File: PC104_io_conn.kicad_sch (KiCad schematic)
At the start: 1 part, among them P651 Conn_04x26_Pin

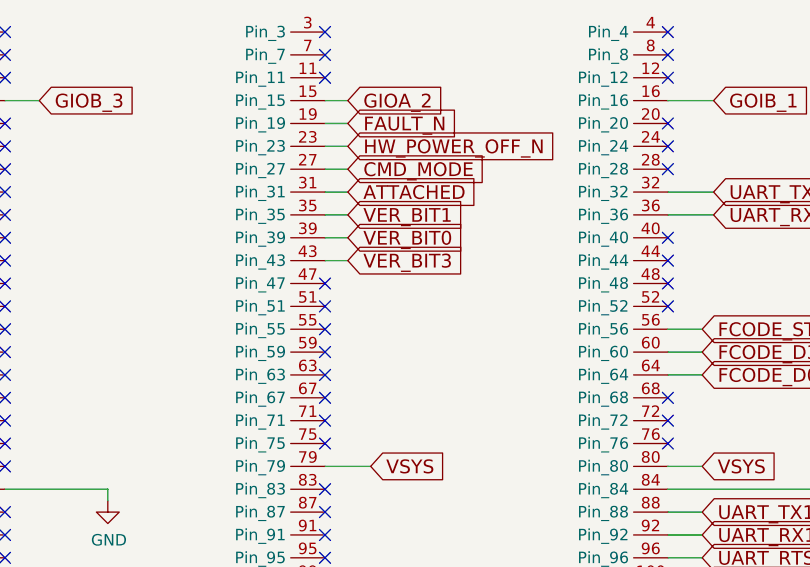
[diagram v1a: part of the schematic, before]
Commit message: Clean up RTC, start working on power
Signed-off-by: Corey Minyard <corey@minyard.net>
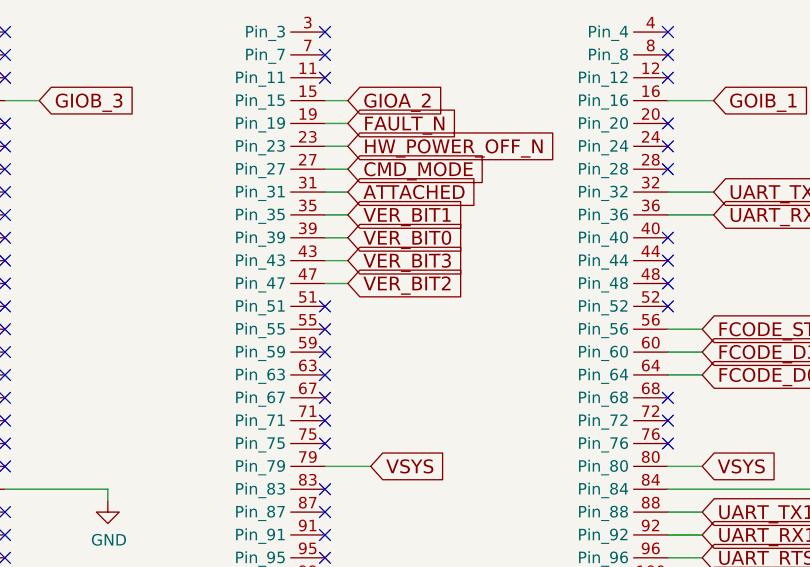
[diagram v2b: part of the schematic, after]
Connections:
- net VER_BIT2: now reaches P651.47 (Pin_47)
- no-connect marks 74 -> 73
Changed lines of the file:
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@@
-	)
-	(no_connect
-		(at 182.88 96.52)
 	)
 	(no_connect
@@
 	(wire
 		(pts
+			(xy 182.88 96.52) (xy 185.42 96.52)
+		)
+		(stroke
+			(width 0)
+			(type default)
+		)
+	)
+	(wire
+		(pts
 			(xy 109.22 96.52) (xy 113.03 96.52)
 		)
@@
 		)
 	)
+	(global_label "VER_BIT2"
+		(shape input)
+		(at 185.42 96.52 0)
+		(fields_autoplaced yes)
+		(effects
+			(font
+				(size 1.524 1.524)
+			)
+			(justify left)
+		)
+		(property "Intersheetrefs" "${INTERSHEET_REFS}"
+			(at 198.4493 96.52 0)
+			(effects
+				(font
+					(size 1.27 1.27)
+				)
+				(justify left)
+				(hide yes)
+			)
+		)
+	)

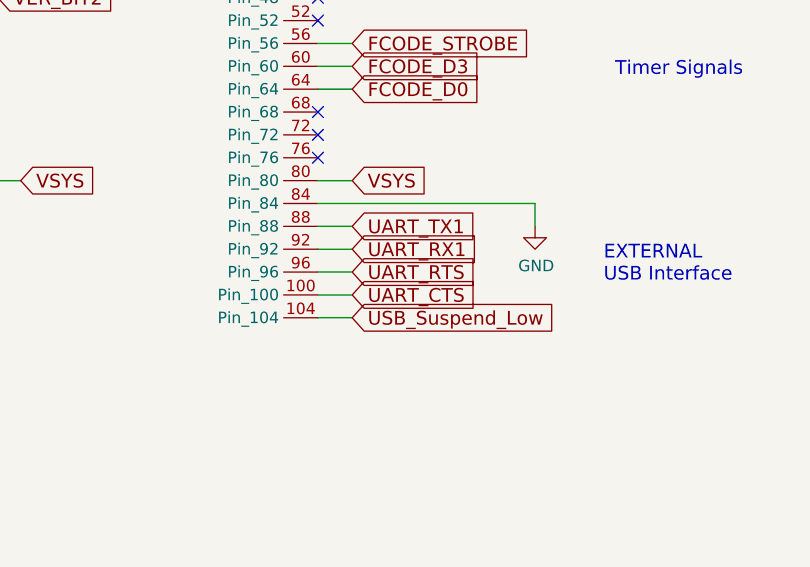
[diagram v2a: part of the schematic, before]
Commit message: More cleanup, finish hooking up power supply controls
Signed-off-by: Corey Minyard <corey@minyard.net>
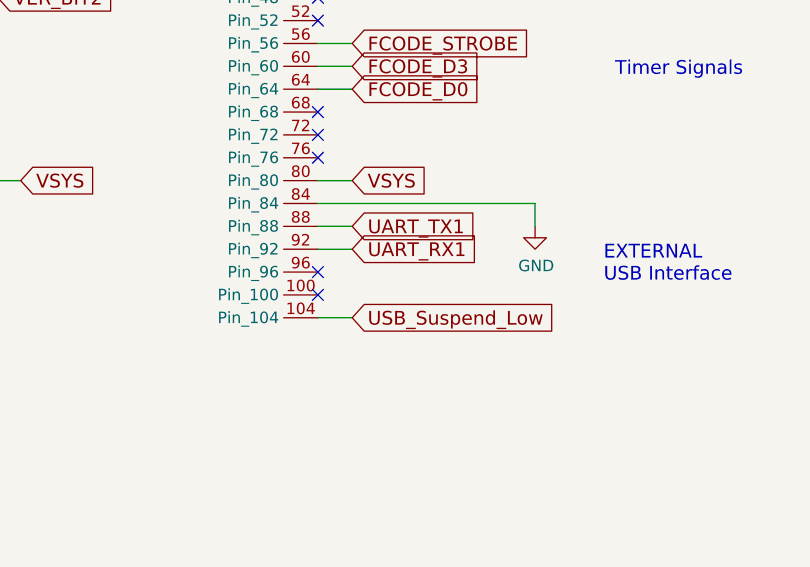
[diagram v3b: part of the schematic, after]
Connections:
- net UART_CTS: no longer names the net of P651.100 (Pin_100)
- net UART_RTS: no longer names the net of P651.96 (Pin_96)
- no-connect marks 73 -> 75
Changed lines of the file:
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@@
+	)
+	(no_connect
+		(at 220.98 129.54)
 	)
 	(no_connect
@@
 	)
 	(no_connect
+		(at 220.98 127)
+	)
+	(no_connect
 		(at 109.22 91.44)
 	)
@@
 	(wire
 		(pts
-			(xy 220.98 127) (xy 224.79 127)
-		)
-		(stroke
-			(width 0)
-			(type default)
-		)
-	)
-	(wire
-		(pts
 			(xy 119.38 69.85) (xy 119.38 73.66)
 		)
@@
 	(wire
 		(pts
-			(xy 220.98 129.54) (xy 224.79 129.54)
-		)
-		(stroke
-			(width 0)
-			(type default)
-		)
-	)
-	(wire
-		(pts
 			(xy 182.88 86.36) (xy 185.42 86.36)
 		)
@@
 		)
 	)
-	(global_label "UART_RTS"
-		(shape input)
-		(at 224.79 127 0)
-		(fields_autoplaced yes)
-		(effects
-			(font
-				(size 1.524 1.524)
-			)
-			(justify left)
-		)
-		(property "Intersheetrefs" "${INTERSHEET_REFS}"
-			(at 238.377 127 0)
-			(effects
-				(font
-					(size 1.27 1.27)
-				)
-				(justify left)
-				(hide yes)
-			)
-		)
-	)
 	(global_label "VER_BIT1"
 		(shape input)
@@
 			(effects
 				(font
-					(size 1.27 1.27)
-				)
-				(justify left)
-				(hide yes)
-			)
-		)
-	)
-	(global_label "UART_CTS"
-		(shape input)
-		(at 224.79 129.54 0)
-		(fields_autoplaced yes)
-		(effects
-			(font
-				(size 1.524 1.524)
-			)
-			(justify left)
-		)
-		(property "Intersheetrefs" "${INTERSHEET_REFS}"
-			(at 238.377 129.54 0)
-			(effects
-				(font

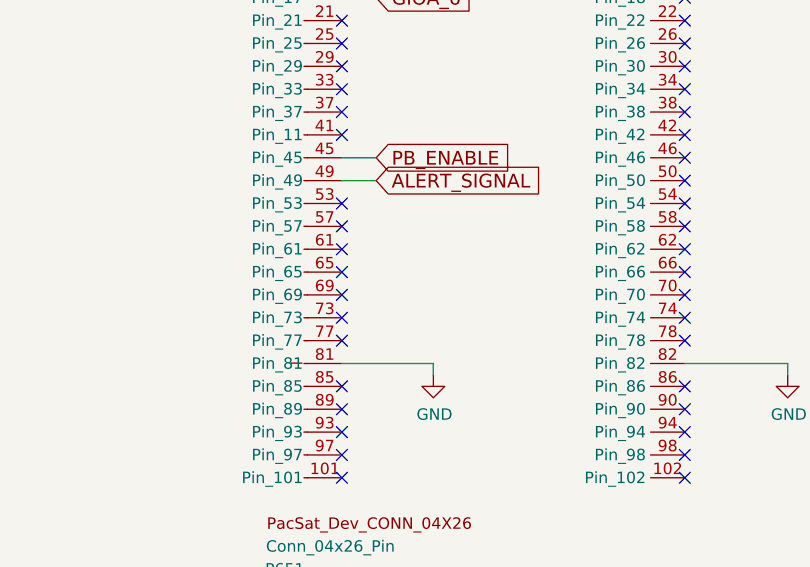
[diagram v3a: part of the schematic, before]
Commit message: Add resistors to the JTAG interface
They are supposed to be there.

Signed-off-by: Corey Minyard <corey@minyard.net>
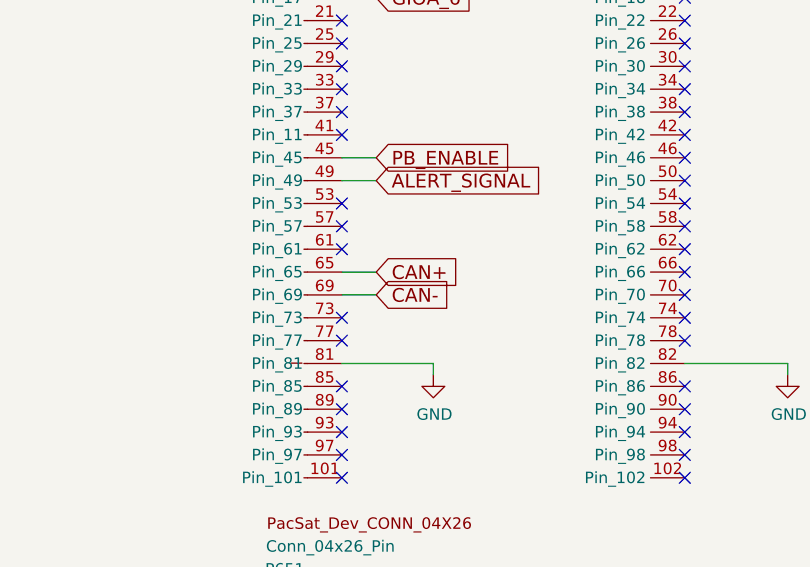
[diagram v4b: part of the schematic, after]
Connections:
- net CAN+: now reaches P651.65 (Pin_65)
- net CAN-: now reaches P651.69 (Pin_69)
- no-connect marks 75 -> 73
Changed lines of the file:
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@@
-	)
-	(no_connect
-		(at 109.22 111.76)
 	)
 	(no_connect
@@
 	)
 	(no_connect
-		(at 109.22 109.22)
-	)
-	(no_connect
 		(at 220.98 81.28)
 	)
@@
 	(wire
 		(pts
+			(xy 109.22 109.22) (xy 113.03 109.22)
+		)
+		(stroke
+			(width 0)
+			(type default)
+		)
+	)
+	(wire
+		(pts
 			(xy 109.22 99.06) (xy 113.03 99.06)
 		)
@@
 		(pts
 			(xy 220.98 121.92) (xy 224.79 121.92)
+		)
+		(stroke
+			(width 0)
+			(type default)
+		)
+	)
+	(wire
+		(pts
+			(xy 109.22 111.76) (xy 113.03 111.76)
 		)
 		(stroke
@@
 			(effects
 				(font
+					(size 1.27 1.27)
+				)
+				(justify left)
+				(hide yes)
+			)
+		)
+	)
+	(global_label "CAN+"
+		(shape input)
+		(at 113.03 109.22 0)
+		(fields_autoplaced yes)
+		(effects
+			(font
+				(size 1.524 1.524)
+			)
+			(justify left)
+		)
+		(property "Intersheetrefs" "${INTERSHEET_REFS}"
+			(at 122.1406 109.22 0)
+			(effects
+				(font
+					(size 1.27 1.27)
+				)
+				(justify left)
+				(hide yes)
+			)
+		)
+	)
+	(global_label "CAN-"
+		(shape input)
+		(at 113.03 111.76 0)
+		(fields_autoplaced yes)
+		(effects
+			(font
+				(size 1.524 1.524)
+			)
+			(justify left)
+		)
+		(property "Intersheetrefs" "${INTERSHEET_REFS}"
+			(at 122.1406 111.76 0)
+			(effects
+				(font

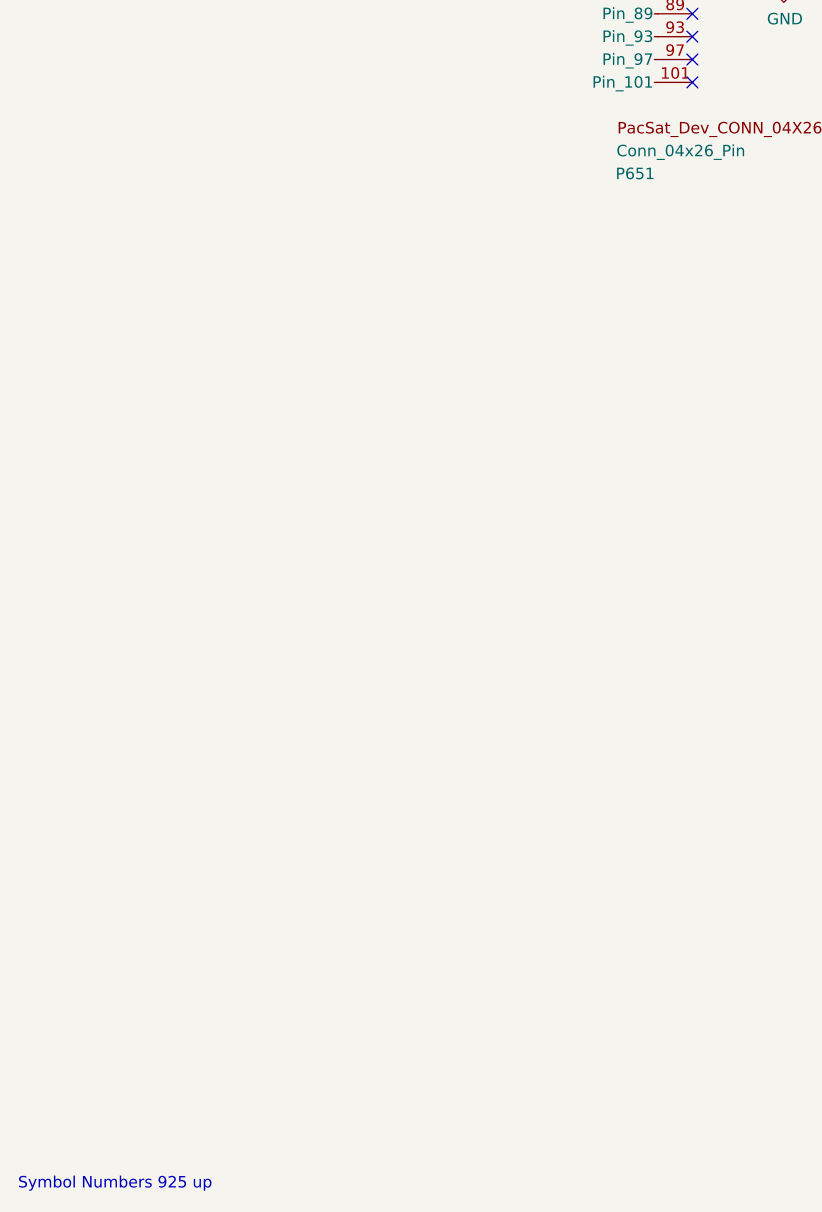
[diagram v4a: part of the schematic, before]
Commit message: Re-annotate all parts
And get rid of the per-sheet annotation remarks.

Signed-off-by: Corey Minyard <corey@minyard.net>
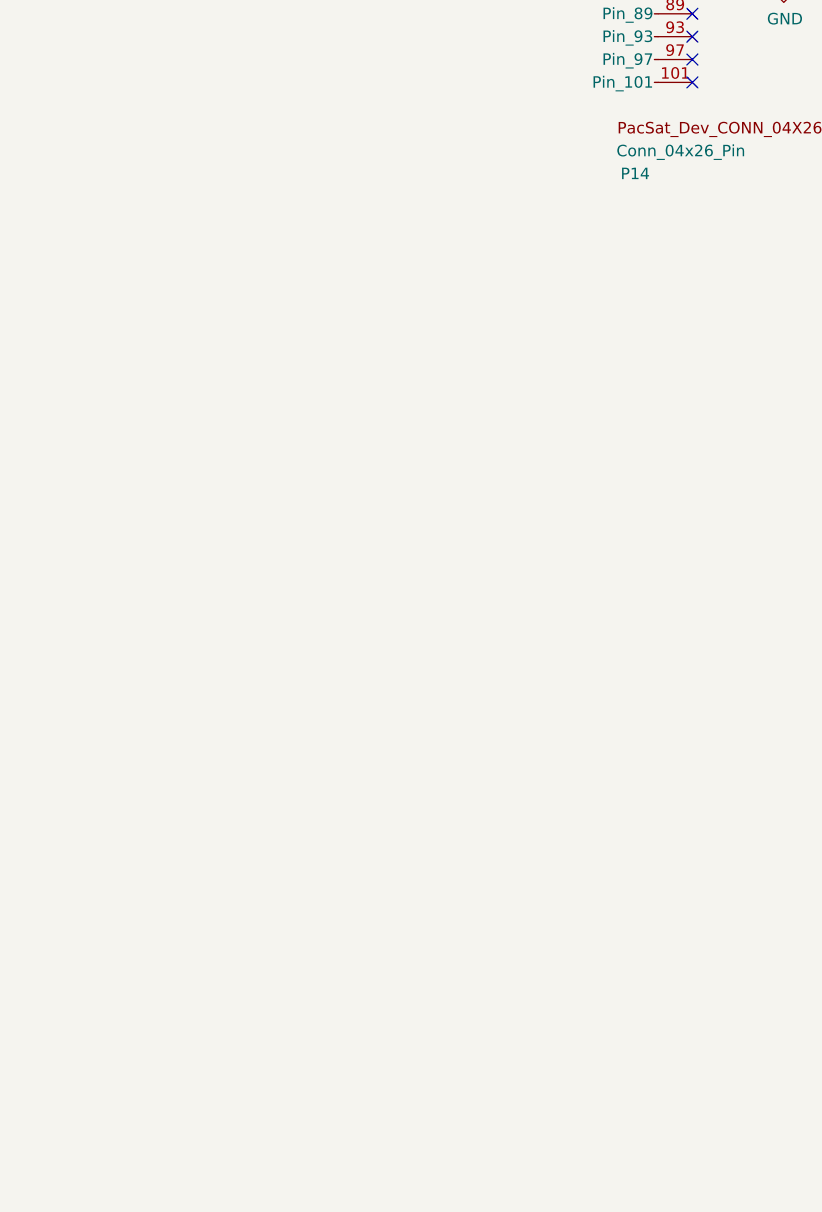
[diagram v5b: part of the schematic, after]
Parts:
- renumbered P651 to P14
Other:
- note removed: "Symbol Numbers 925 up"
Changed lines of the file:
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@@
-		)
-	)
-	(text "Symbol Numbers 925 up"
-		(exclude_from_sim no)
-		(at 34.29 255.27 0)
-		(effects
-			(font
-				(size 1.27 1.27)
-			)
-			(justify left bottom)
 		)
 	)
@@
 		(dnp no)
 		(fields_autoplaced yes)
-		(property "Reference" "#PWR0624"
+		(property "Reference" "#PWR0236"
 			(at 119.38 73.66 0)
 			(effects
@@
 			(project "PacSat_Dev_RevD_240614"
 				(path "/cc9f42d2-6985-41ac-acab-5ab7b01c5b38/163b95be-82a7-4cd3-9077-48a01f79e25c"
-					(reference "#PWR0624")
+					(reference "#PWR0236")
 					(unit 1)
 				)
@@
 		(on_board yes)
 		(dnp no)
-		(property "Reference" "#PWR0622"
+		(property "Reference" "#PWR0238"
 			(at 158.75 127 0)
 			(effects
@@
 			(project "PacSat_Dev_RevD_240614"
 				(path "/cc9f42d2-6985-41ac-acab-5ab7b01c5b38/163b95be-82a7-4cd3-9077-48a01f79e25c"
-					(reference "#PWR0622")
+					(reference "#PWR0238")
 					(unit 1)
 				)
@@
 		(on_board yes)
 		(dnp no)
-		(property "Reference" "#PWR036"
+		(property "Reference" "#PWR0239"
 			(at 245.11 128.27 0)
 			(effects
@@
 			(project "PacSat_Dev_RevD_240614"
 				(path "/cc9f42d2-6985-41ac-acab-5ab7b01c5b38/163b95be-82a7-4cd3-9077-48a01f79e25c"
-					(reference "#PWR036")
+					(reference "#PWR0239")
 					(unit 1)
 				)
@@
 		(dnp no)
 		(fields_autoplaced yes)
-		(property "Reference" "#PWR038"
+		(property "Reference" "#PWR0235"
 			(at 113.03 68.58 0)
 			(effects
@@
 			(project "PacSat_Dev_RevD_240614"
 				(path "/cc9f42d2-6985-41ac-acab-5ab7b01c5b38/163b95be-82a7-4cd3-9077-48a01f79e25c"
-					(reference "#PWR038")
+					(reference "#PWR0235")
 					(unit 1)
 				)
@@
 		(on_board yes)
 		(dnp no)
-		(property "Reference" "P651"
+		(property "Reference" "P14"
 			(at 102.87 142.24 0)
 			(effects
@@
 			(project "PacSat_Dev_RevD_240614"
 				(path "/cc9f42d2-6985-41ac-acab-5ab7b01c5b38/163b95be-82a7-4cd3-9077-48a01f79e25c"
-					(reference "P651")
+					(reference "P14")
 					(unit 1)
 				)
@@
 		(on_board yes)
 		(dnp no)
-		(property "Reference" "#PWR0623"
+		(property "Reference" "#PWR0237"
 			(at 119.38 127 0)
 			(effects
@@
 			(project "PacSat_Dev_RevD_240614"
 				(path "/cc9f42d2-6985-41ac-acab-5ab7b01c5b38/163b95be-82a7-4cd3-9077-48a01f79e25c"
-					(reference "#PWR0623")
+					(reference "#PWR0237")
 					(unit 1)
 				)

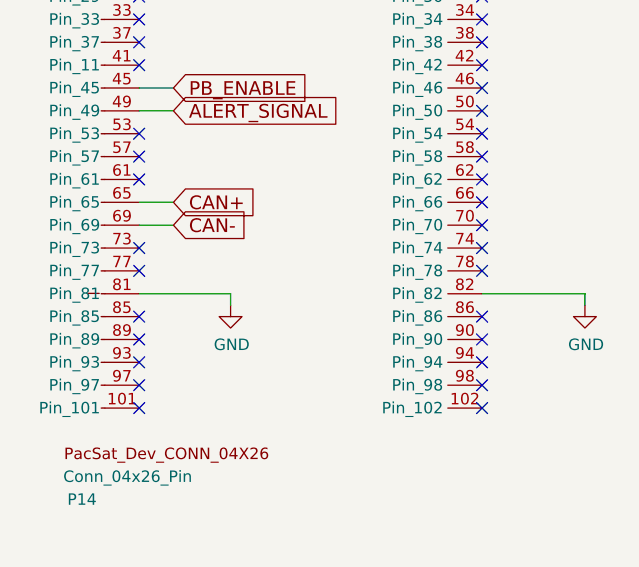
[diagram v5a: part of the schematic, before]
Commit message: Add a second CAN bus interface
Redundancy...

Signed-off-by: Corey Minyard <corey@minyard.net>
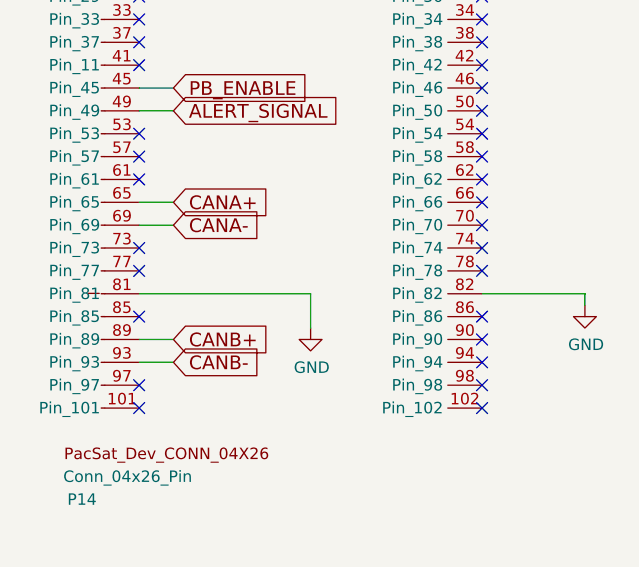
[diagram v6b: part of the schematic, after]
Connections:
- net CANB+: now reaches P14.89 (Pin_89)
- net CANB-: now reaches P14.93 (Pin_93)
- net CAN+ renamed CANA+
- net CAN- renamed CANA-
- no-connect marks 73 -> 71
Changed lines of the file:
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@@
-	)
-	(no_connect
-		(at 109.22 124.46)
 	)
 	(no_connect
@@
 	)
 	(no_connect
-		(at 109.22 127)
-	)
-	(no_connect
 		(at 147.32 104.14)
 	)
@@
 	(wire
 		(pts
-			(xy 109.22 119.38) (xy 119.38 119.38)
+			(xy 109.22 119.38) (xy 128.27 119.38)
 		)
 		(stroke
@@
 	(wire
 		(pts
+			(xy 109.22 127) (xy 113.03 127)
+		)
+		(stroke
+			(width 0)
+			(type default)
+		)
+	)
+	(wire
+		(pts
 			(xy 113.03 64.77) (xy 113.03 68.58)
 		)
@@
 	(wire
 		(pts
-			(xy 119.38 119.38) (xy 119.38 120.65)
+			(xy 128.27 119.38) (xy 128.27 123.19)
 		)
 		(stroke
@@
 	(wire
 		(pts
+			(xy 109.22 124.46) (xy 113.03 124.46)
+		)
+		(stroke
+			(width 0)
+			(type default)
+		)
+	)
+	(wire
+		(pts
 			(xy 119.38 69.85) (xy 119.38 73.66)
 		)
@@
 		)
 	)
-	(global_label "CAN+"
+	(global_label "CANA+"
 		(shape input)
 		(at 113.03 109.22 0)
@@
 		)
 		(property "Intersheetrefs" "${INTERSHEET_REFS}"
-			(at 122.1406 109.22 0)
-			(effects
-				(font
-					(size 1.27 1.27)
-				)
-				(justify left)
-				(hide yes)
-			)
-		)
-	)
-	(global_label "CAN-"
+			(at 123.4469 109.22 0)
+			(effects
+				(font
+					(size 1.27 1.27)
+				)
+				(justify left)
+				(hide yes)
+			)
+		)
+	)
+	(global_label "CANA-"
 		(shape input)
 		(at 113.03 111.76 0)
@@
 		)
 		(property "Intersheetrefs" "${INTERSHEET_REFS}"
-			(at 122.1406 111.76 0)
+			(at 123.4469 111.76 0)
 			(effects
 				(font
@@
 		)
 	)
+	(global_label "CANB-"
+		(shape input)
+		(at 113.03 127 0)
+		(fields_autoplaced yes)
+		(effects
+			(font
+				(size 1.524 1.524)
+			)
+			(justify left)
+		)
+		(property "Intersheetrefs" "${INTERSHEET_REFS}"
+			(at 123.6646 127 0)
+			(effects
+				(font
+					(size 1.27 1.27)
+				)
+				(justify left)
+				(hide yes)
+			)
+		)
+	)
 	(global_label "CMD_MODE"
 		(shape input)
@@
 		(property "Intersheetrefs" "${INTERSHEET_REFS}"
 			(at 238.6673 124.46 0)
+			(effects
+				(font
+					(size 1.27 1.27)
+				)
+				(justify left)
+				(hide yes)
+			)
+		)
+	)
+	(global_label "CANB+"
+		(shape input)
+		(at 113.03 124.46 0)
+		(fields_autoplaced yes)
+		(effects
+			(font
+				(size 1.524 1.524)
+			)
+			(justify left)
+		)
+		(property "Intersheetrefs" "${INTERSHEET_REFS}"
+			(at 123.6646 124.46 0)
 			(effects
 				(font
@@
 	(symbol
 		(lib_id "power:GND")
-		(at 119.38 120.65 0)
+		(at 128.27 123.19 0)
 		(unit 1)
 		(exclude_from_sim no)
@@
 		(dnp no)
 		(property "Reference" "#PWR0237"
-			(at 119.38 127 0)
+			(at 128.27 129.54 0)
 			(effects
 				(font
@@
 		)
 		(property "Value" "GND"
-			(at 119.507 125.0442 0)
+			(at 128.397 127.5842 0)
 			(effects
 				(font
@@
 		)
 		(property "Footprint" ""
-			(at 119.38 120.65 0)
+			(at 128.27 123.19 0)
 			(effects
 				(font
@@
 		)
 		(property "Datasheet" ""
-			(at 119.38 120.65 0)
+			(at 128.27 123.19 0)
 			(effects
 				(font
@@
 		)
 		(property "Description" ""
-			(at 119.38 120.65 0)
-			(effects
-				(font
+			(at 128.27 123.19 0)
+			(effects
+				(font
